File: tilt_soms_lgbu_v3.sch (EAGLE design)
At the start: 30 parts

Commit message: edc modules - larger pad size for dcdc gateway - right package for capacitor and fuse tilt board - no more timer module, embedded design, right packages for caps and fuse
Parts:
- removed C8: (no value), rcl:C-USC1812
- removed FUSE1: MF-SMDF200, fuse:MF-SMDF200
- removed U$3: TPL5110_BREAKOUT, edc_modules:TPL5110_BREAKOUT
- added C6: 0.1uF, rcl:C-EUC0402
- added C9: (no value), microbuilder:CAP_TANTALUMA/3216_WAVE
- added EN, MISO, MOSI, SCK: (no value), microbuilder:TESTPOINTROUND2MM
- added PTC1: (no value), microbuilder:PTC1210
- added Q1: CMG3415, microbuilder:MOSFET-PWIDE
- added R2: (no value), microbuilder:RESISTOR0805
- added TIMER: TPL5110, edc_modules:TPL5110
- added TRIG: (no value), microbuilder:SOLDERJUMPER
- C5, C7: device rcl:C-USC1812 -> rcl:C-USC1206K
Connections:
- removed net VOLTAGE_SUPPLY: C7.1, C8.1, FUSE1.2, U$3.VDD
- new net N$6: Q1.G, TIMER.DRVN
- new net VBAT: C6.1, C7.1, PTC1.1, Q1.S, TIMER.EN, TIMER.VDD, TRIG.2
- net CSB_EN: now also EN.P$1
- net DELAY: now also TIMER.DELAY, TRIG.1; no longer U$3.DELAY
- net DONE_PIN: now also R2.2, TIMER.DONE; no longer U$3.DONE
- net FEATHER_BAT: now also C9.+, Q1.D; no longer U$3.DRV
- net GND: now also C6.2, C9.-, R2.1, TIMER.GND; no longer C8.2, U$3.GND
- net MISO: now also MISO.P$1
- net MOSI: now also MOSI.P$1
- net N$4: now also PTC1.2; no longer FUSE1.1
- net SCK: now also SCK.P$1
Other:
- moved on the sheet: C7, R1

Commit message: ferrite bead, pull ups, standard battery header
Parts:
- removed MAIN_SWITCH: JST-PH_2-PIN_HEADER, SRG:JST-PH_2-PIN_HEADER
- added L1: BLM15HG601SN1, inductors:BLM15HG601SN1
- added MAINS: JST-PH_2-PIN_HEADER, SRG:JST-PH_2-PIN_HEADER
- added R3, R4: (no value), microbuilder:RESISTOR0805
- added TRIG_TEST: (no value), microbuilder:SOLDERJUMPER
- BATT: value JST-PH_2-PIN_HEADER -> (none); device SRG:JST-PH_2-PIN_HEADER -> SparkFun-Connectors:CONN_02POLAR_LOCK
- R1: device rcl:R-EU_0207/7 -> rcl:R-EU_0207/10
- TRIG: value (none) -> JST-PH_2-PIN_HEADER; device microbuilder:SOLDERJUMPER -> SRG:JST-PH_2-PIN_HEADER
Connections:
- new net N$7: C1.1, C5.1, INCLINOMETER.VDD, L1.1
- net +3V3: now also L1.2, R3.2, R4.2; no longer C1.1, C5.1, INCLINOMETER.VDD
- net DELAY: now also TRIG_TEST.1
- net GND: now also BATT.2; no longer BATT.1
- net MISO: now also R3.1
- net MOSI: now also R4.1
- net N$3: now also BATT.1, MAINS.1; no longer BATT.2, MAIN_SWITCH.1
- net N$4: now also MAINS.2; no longer MAIN_SWITCH.2
- net VBAT: now also TRIG_TEST.2
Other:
- moved on the sheet: C1, C2, C3, C4, C5, C6, C7, C9, EN, INCLINOMETER, MISO, MOSI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

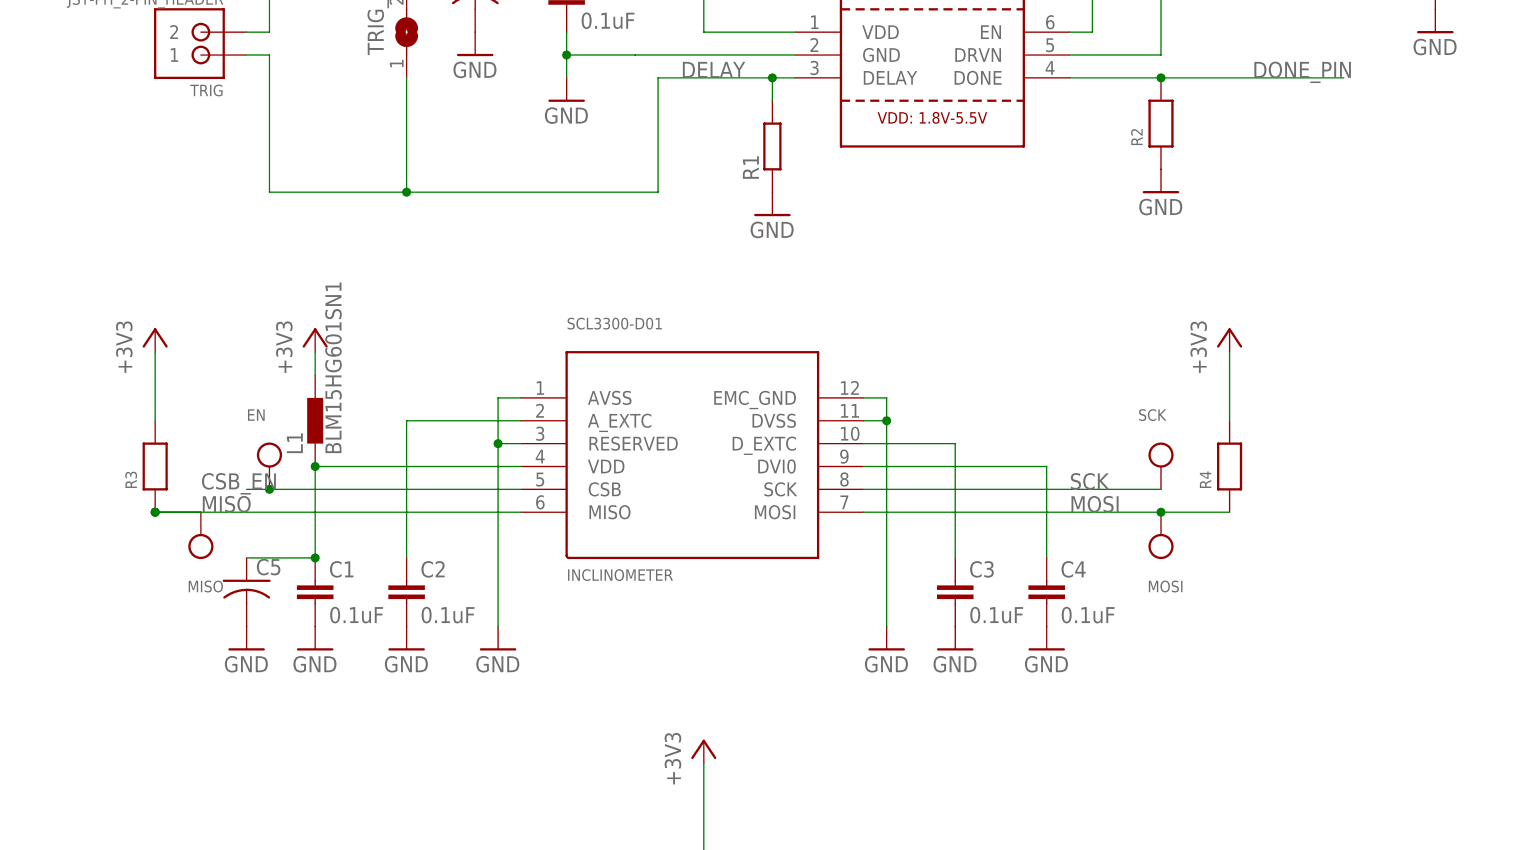
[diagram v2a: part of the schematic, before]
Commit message: lengthen scl3300 pads, isolated pads for axel, all supply goes through a ferrite bead
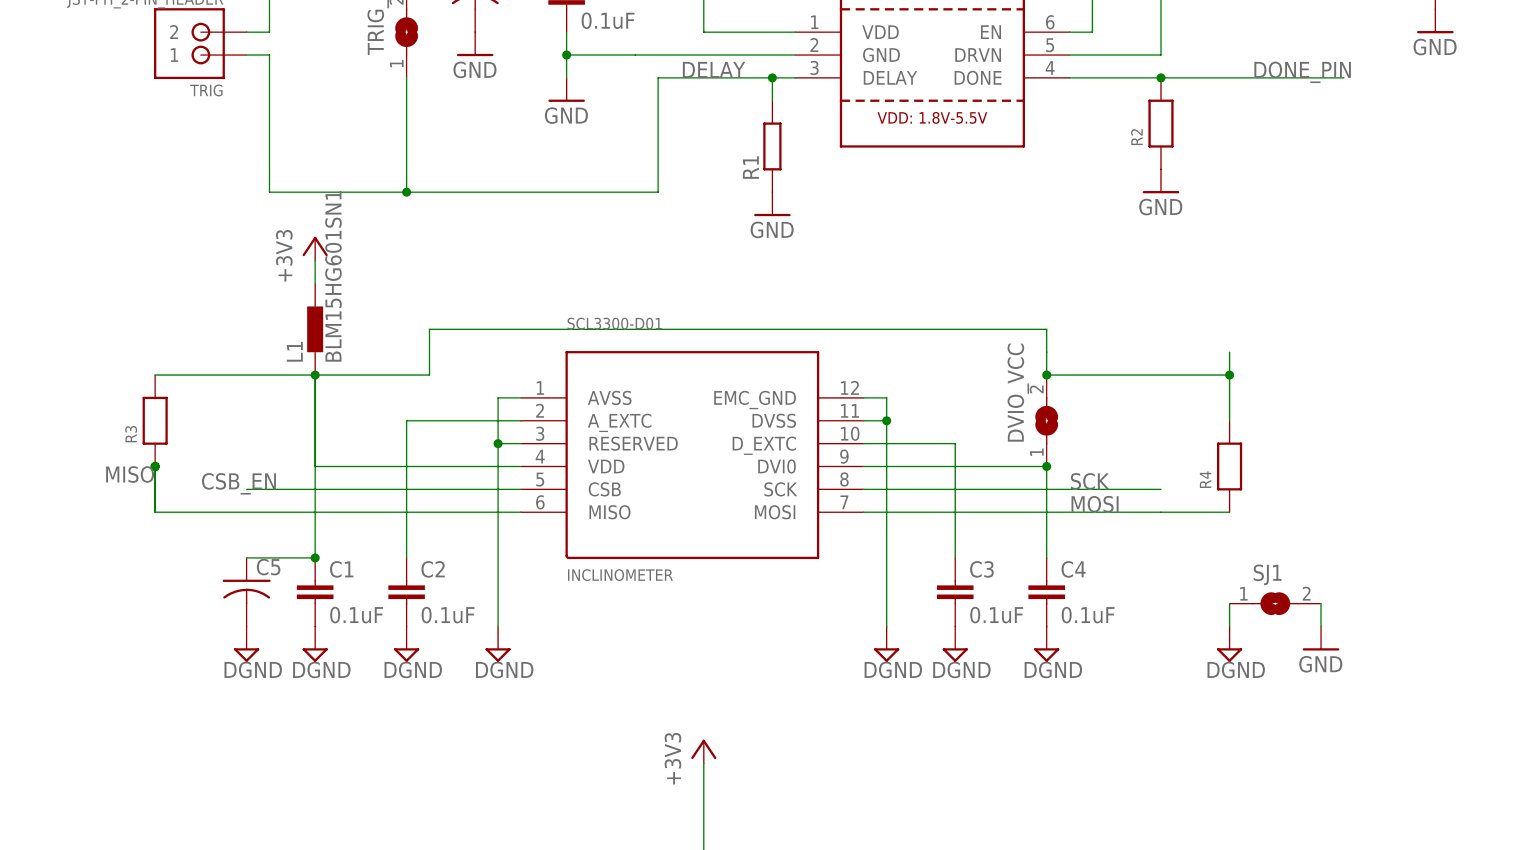
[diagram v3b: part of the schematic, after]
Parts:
- removed EN, MISO, MOSI, SCK: (no value), microbuilder:TESTPOINTROUND2MM
- added DVIO_VCC: (no value), microbuilder:SOLDERJUMPER
- added SJ1: (no value), jumper:SJ
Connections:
- new net DGND: C1.2, C2.2, C3.2, C4.2, C5.2, INCLINOMETER.AVSS, INCLINOMETER.DVSS, INCLINOMETER.EMC_GND, INCLINOMETER.RESERVED, SJ1.1
- net +3V3: no longer R3.2, R4.2
- net CSB_EN: no longer EN.P$1
- net GND: now also SJ1.2; no longer C1.2, C2.2, C3.2, C4.2, C5.2, INCLINOMETER.AVSS, INCLINOMETER.DVSS, INCLINOMETER.EMC_GND, INCLINOMETER.RESERVED
- net MISO: no longer MISO.P$1
- net MOSI: no longer MOSI.P$1
- net N$5: now also DVIO_VCC.1
- net N$7: now also DVIO_VCC.2, R3.2, R4.2
- net SCK: no longer SCK.P$1
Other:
- moved on the sheet: L1, R3
